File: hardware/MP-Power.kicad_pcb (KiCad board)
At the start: 2 copper layers, 17 x 15.7 mm, 12 parts, among them U1 MP1584EN

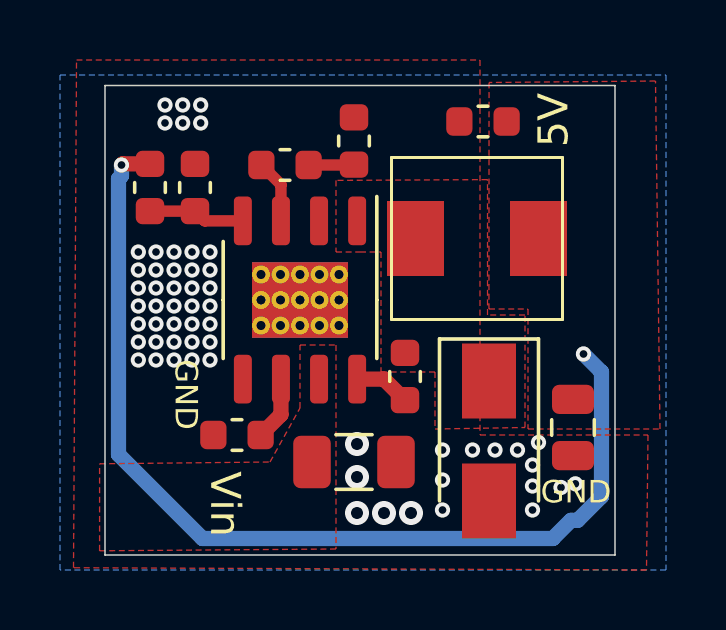
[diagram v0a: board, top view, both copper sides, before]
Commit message: Copy the power converter.
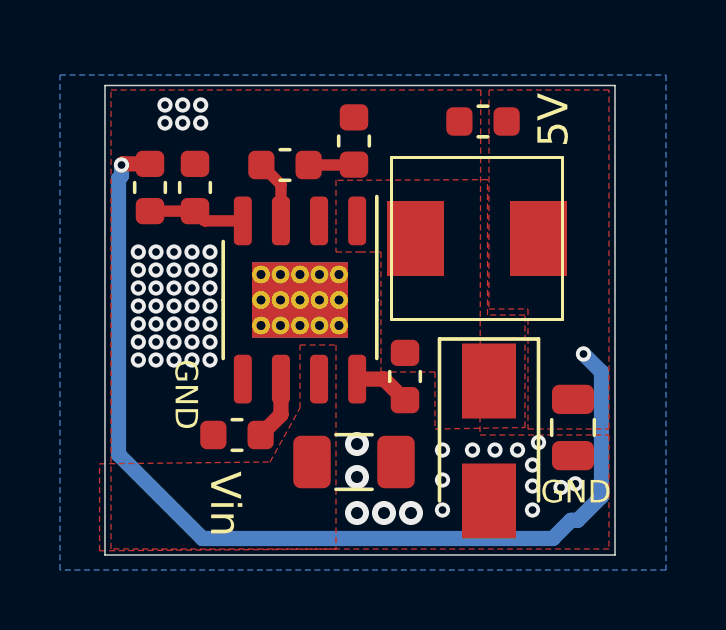
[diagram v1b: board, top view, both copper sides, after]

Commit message: Select better schottky diode.
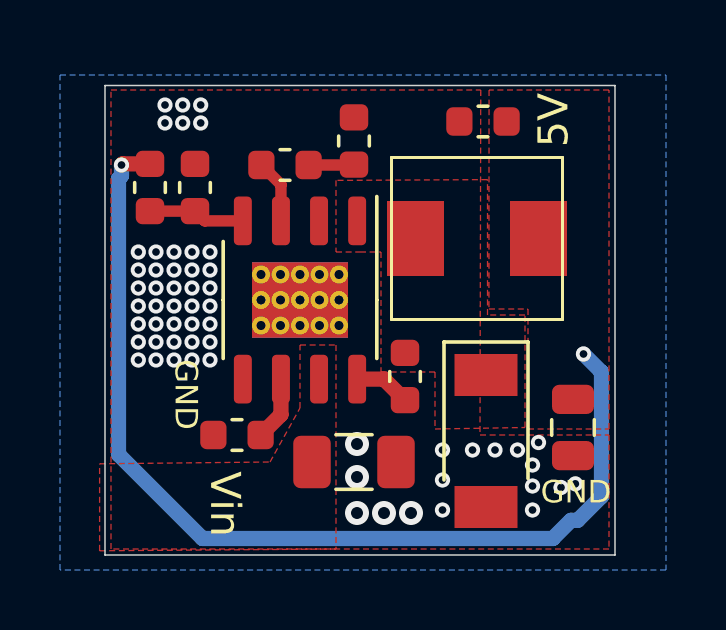
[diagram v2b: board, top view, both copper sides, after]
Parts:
- D1: value SS34 -> PMEG3050EP; footprint Diode_SMD:D_SMA -> PrntrBoardV2:SOD-128
- moved D1 0.10 mm to (120.2, 83.2)
